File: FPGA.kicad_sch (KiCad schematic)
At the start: 47 parts, among them IC10 ICE5LP4K-SG48I, IC11 MT25QL128ABA1ESE-0SIT, J12 SAMTEC_HTSW-101-23-L-D, J13 SAMTEC_HTSW-105-23-L-D, J14 SAMTEC_HTSW-101-23-L-D, J15 SAMTEC_SSW-106-02-L-D-RA, J16 SAMTEC_SSW-106-02-L-D-RA, SW6 HARWIN_M50-1900005

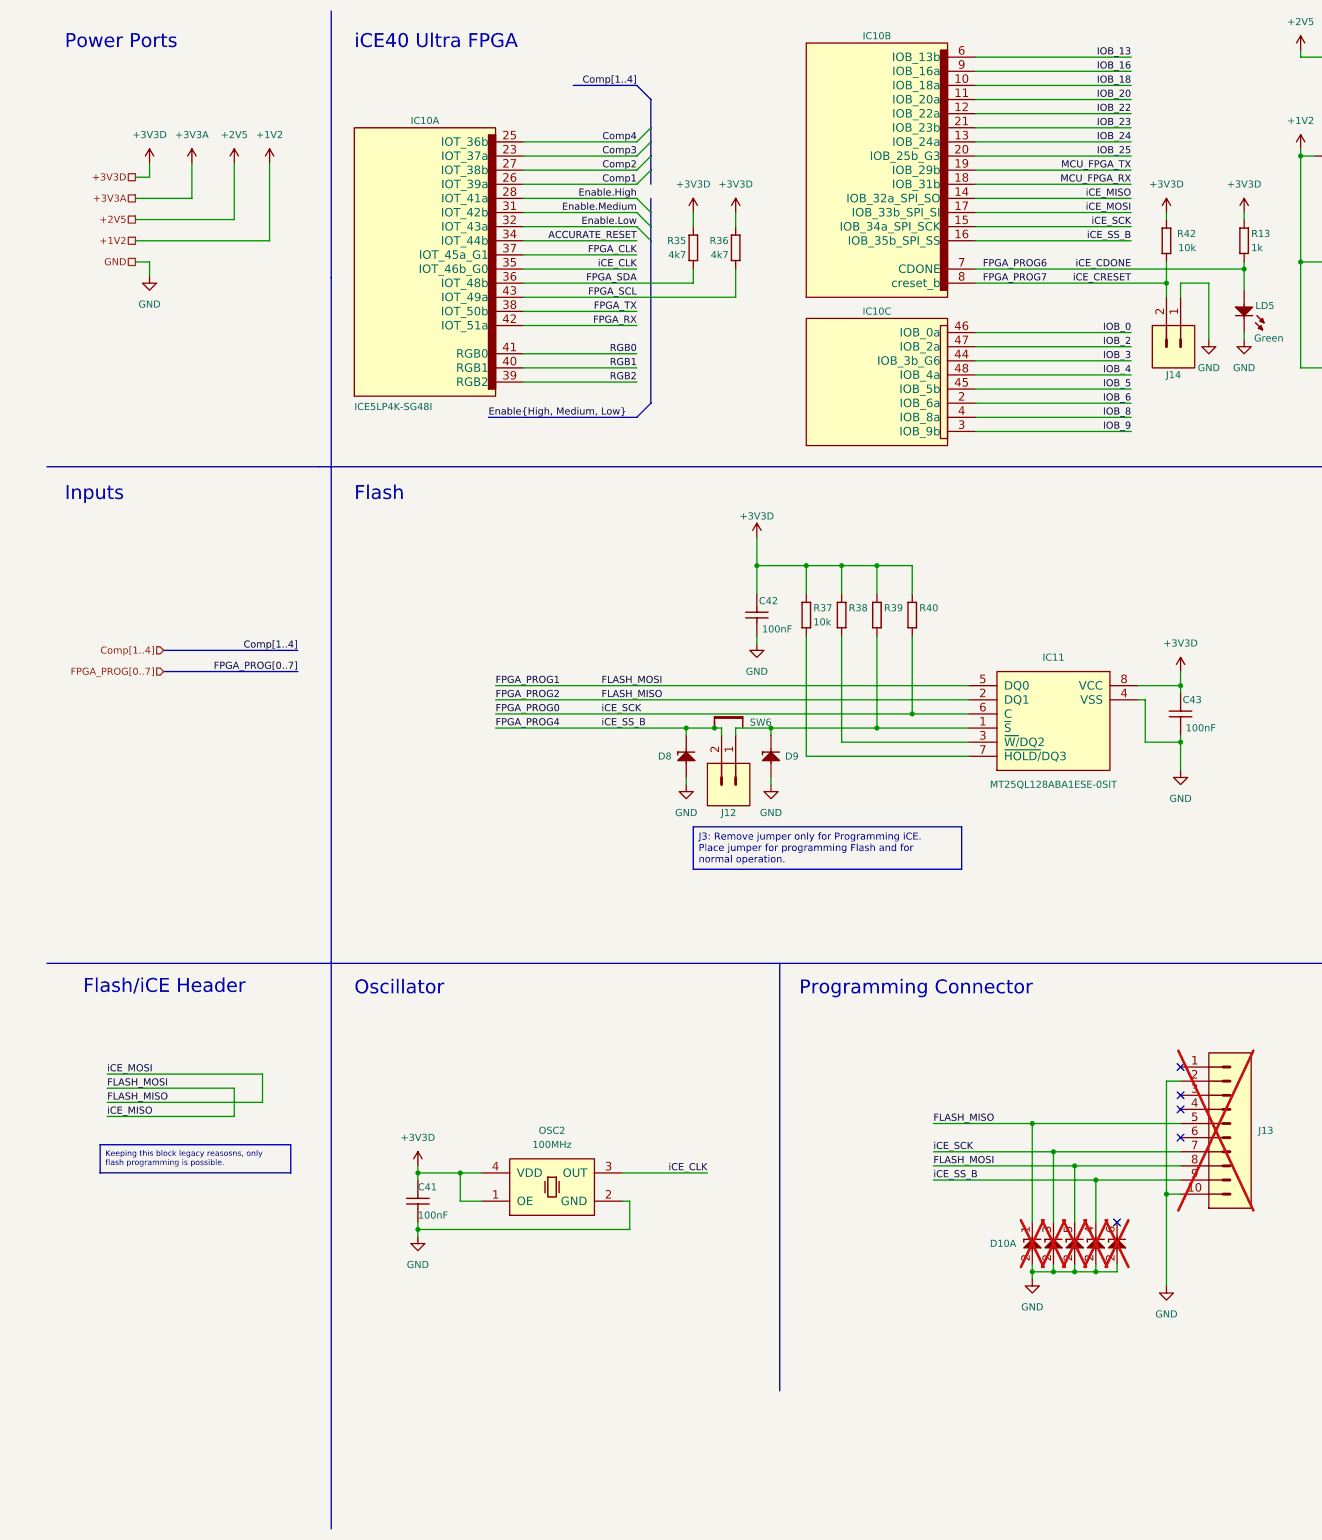
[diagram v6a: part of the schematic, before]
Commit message: Rename FPGA_PROG bus for mor clarity + small changes
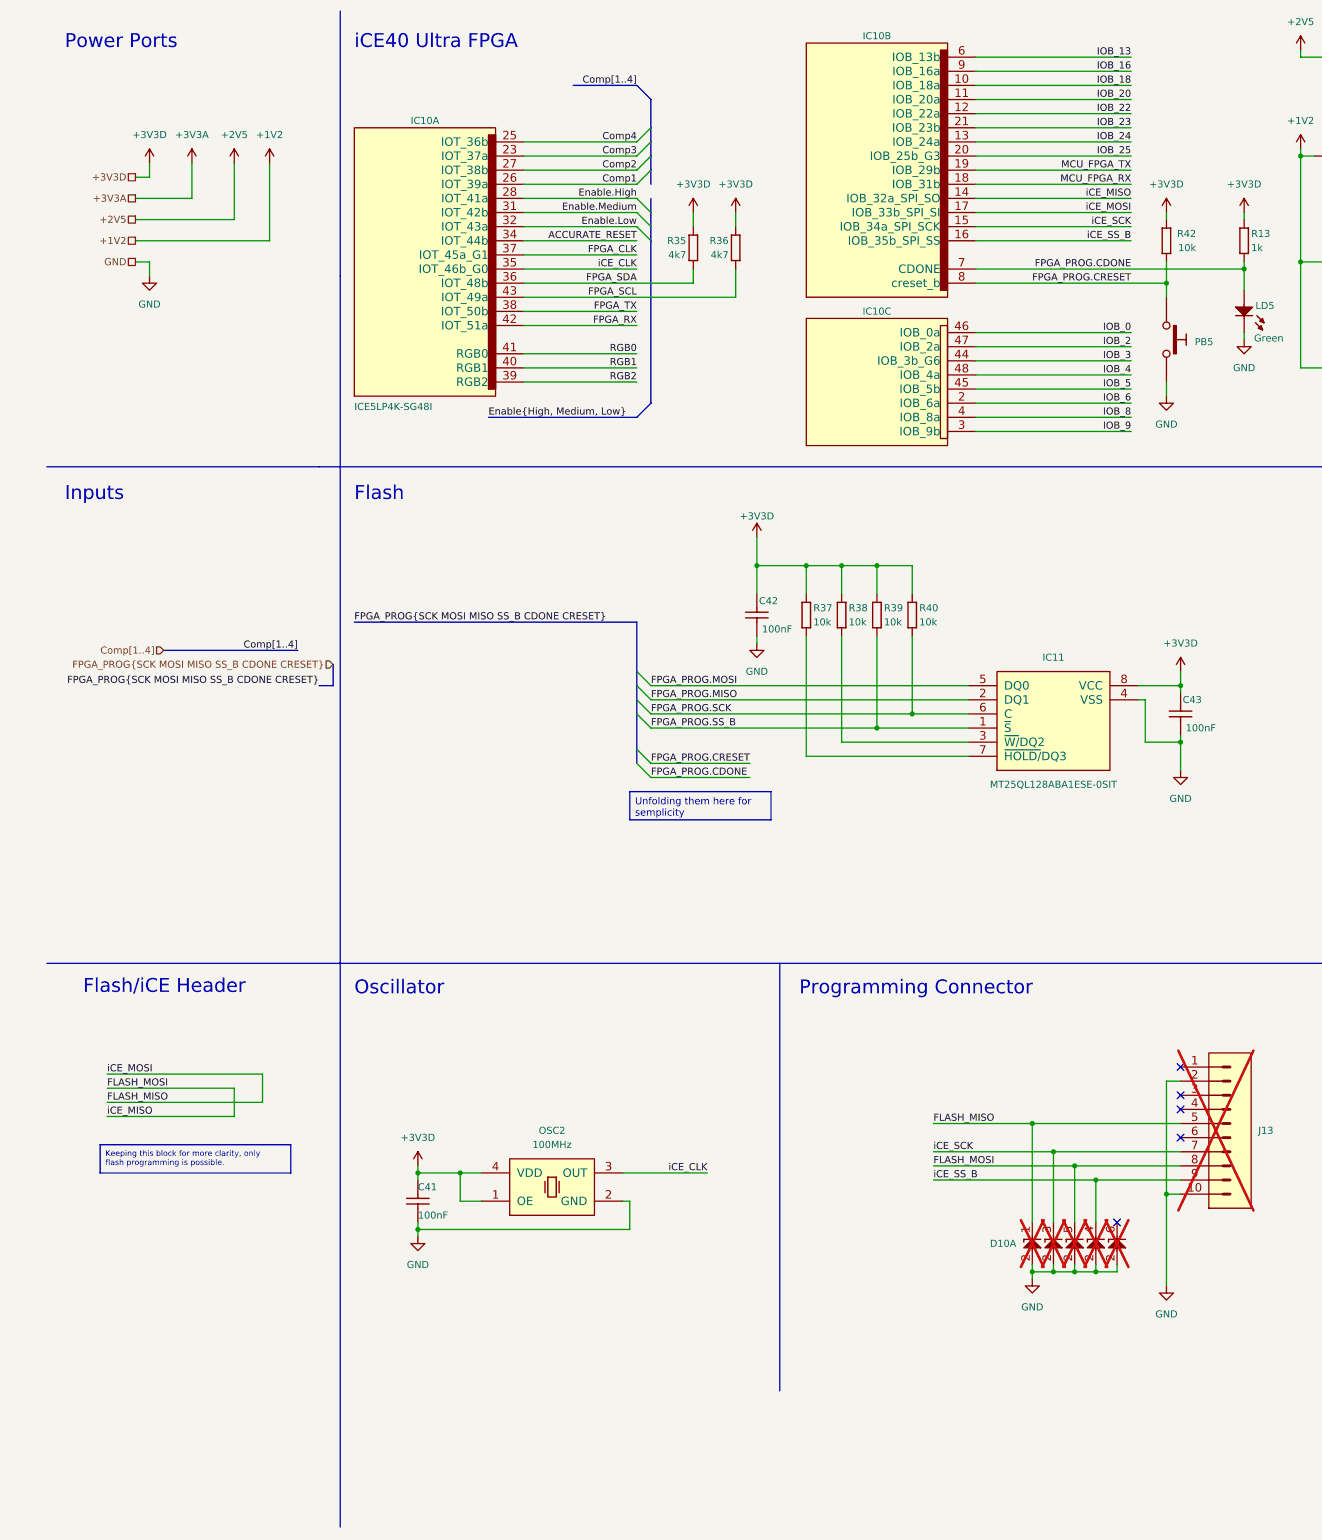
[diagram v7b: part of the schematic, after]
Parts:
- removed D8, D9: PESD3V3S1UB, ICs And Semiconductors SMD:SODFL1608X65N, symbol Diodes:PESD3V3S1UB
- removed J12, J14: SAMTEC_HTSW-101-23-L-D, SAMTEC THD:SAMTEC_HTSW-101-23-L-D, symbol SAMTEC:SAMTEC_HTSW-101-23-L-D
- removed SW6: HARWIN_M50-1900005, COMATEL THD:STELVIO-KONTEK_3131730000400, symbol STELVIO-KONTEK COMATEL:STELVIO-KONTEK_3131730000400
- added PB5: PB_C&K_KSC321JLFS, Switches:PB_C&K_KSC321J, symbol Switches:PB_C&K_KSC321JLFS
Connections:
- net FLASH_MISO: no longer IC11.2 (DQ1)
- net FLASH_MOSI: no longer IC11.5 (DQ0)
- net GND: now also PB5.3, PB5.4
- net FPGA_PROG.SS_B: now reaches IC11.1 (~{S}), R39.1
- net FPGA_PROG0 renamed iCE_SCK
- net iCE_SCK: no longer IC11.6 (C), R40.1
- net FPGA_PROG4 renamed iCE_SS_B
- net FPGA_PROG6 renamed FPGA_PROG.CDONE
- net FPGA_PROG7 renamed FPGA_PROG.CRESET
- net FPGA_PROG.CRESET: now also PB5.1, PB5.2
- new net FPGA_PROG.MISO: IC11.2 (DQ1)
- new net FPGA_PROG.MOSI: IC11.5 (DQ0)
- new net FPGA_PROG.SCK: IC11.6 (C), R40.1

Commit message: I forgot what I've done here. Close to done
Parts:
- added D3: PESD3V3L5UY, ICs And Semiconductors SMD:SOT65P210X110-6N, symbol Diodes:PESD3V3L5UY
- added D7: PESD3V3S1UB, ICs And Semiconductors SMD:SODFL1608X65N, symbol Diodes:PESD3V3S1UB
- added J11: SAMTEC_HTSW-103-23-L-D, SAMTEC THD:SAMTEC_HTSW-103-23-L-D, symbol SAMTEC:SAMTEC_HTSW-103-23-L-D
- added SW4, SW5: HARWIN_M50-1900005, COMATEL THD:STELVIO-KONTEK_3131730000400, symbol STELVIO-KONTEK COMATEL:STELVIO-KONTEK_3131730000400
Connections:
- net GND: now also D3.2 (A), D3.2 (A), D3.2 (A), D3.2 (A), D3.2 (A), D7.2 (A)
- net IOB_18: no longer PB6.1, PB6.2, R66.2
- net FPGA_RX renamed FPGA_UART.RX
- net FPGA_UART.RX: now also D3.5 (C), J11.4
- net FPGA_TX renamed FPGA_UART.TX
- net FPGA_UART.TX: now also D3.4 (C), J11.3
- net MCU_FPGA_RX renamed ADC_Ready
- net MCU_FPGA_TX renamed FPGA_RESET
- net FPGA_RESET: now also PB6.1, PB6.2, R66.2
- new net FPGA_FTDI_UART_RX: D7.1 (C), J11.6
- new net FPGA_FTDI_UART_TX: D3.6 (C), J11.5
- new net FPGA_MCU_UART_RX: D3.3 (C), J11.2, SW5.1
- new net FPGA_MCU_UART_TX: D3.1 (C), J11.1, SW4.1
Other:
- note added: "FTDI/MCU UART Header"
- moved on the sheet: C41, OSC2
